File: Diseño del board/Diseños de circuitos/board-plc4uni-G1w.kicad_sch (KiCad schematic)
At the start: 0 parts

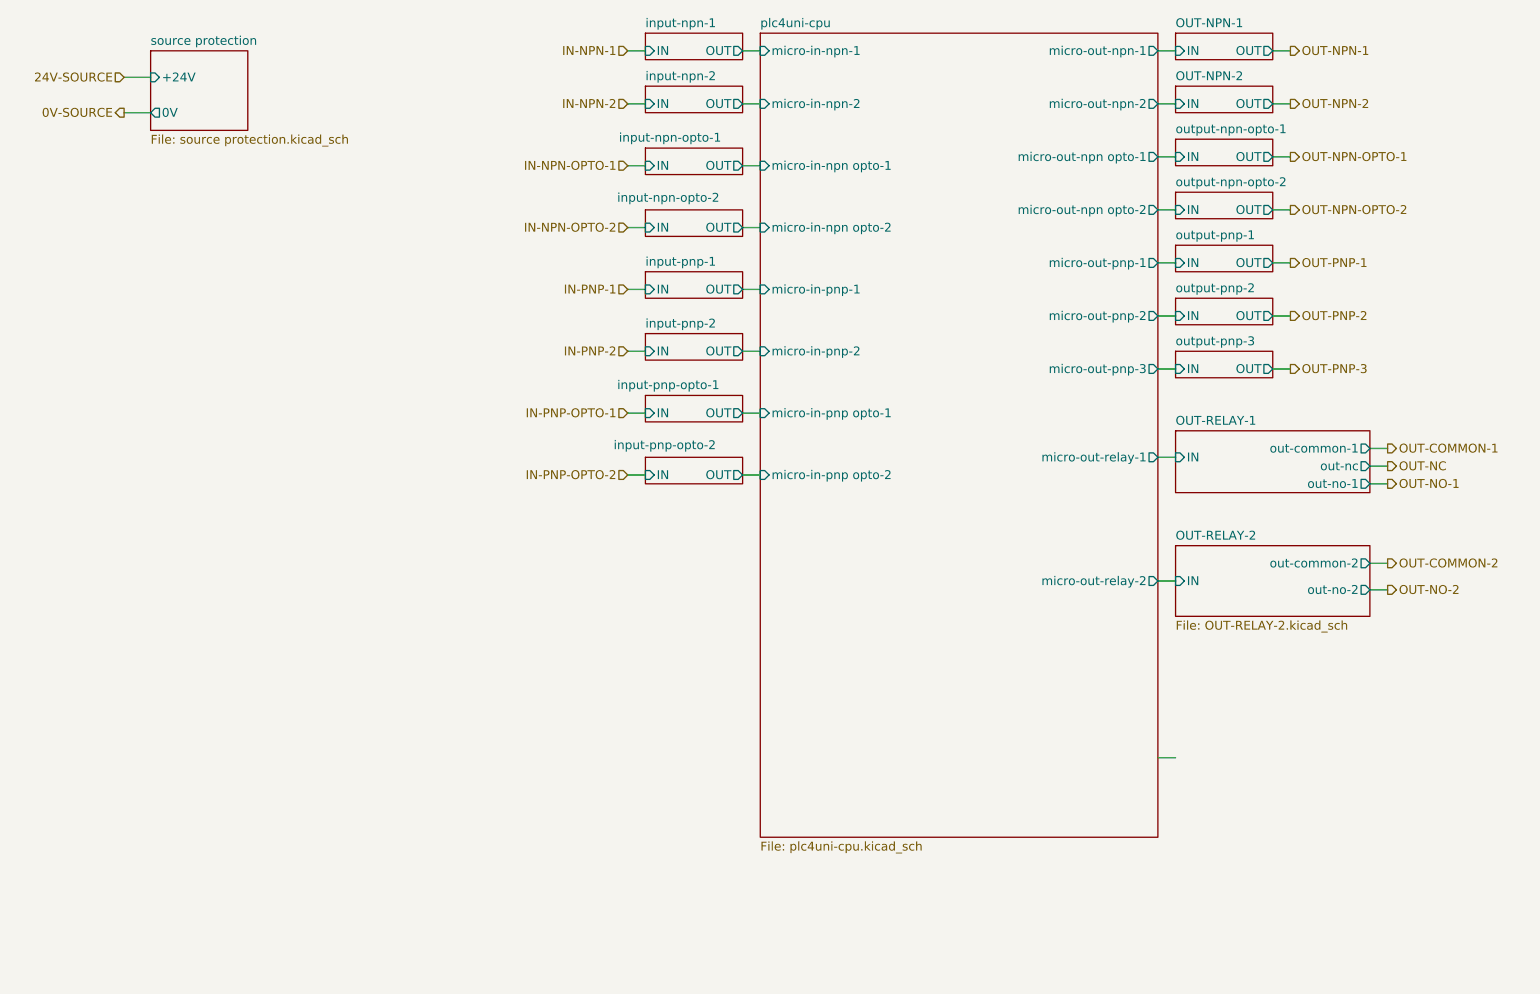
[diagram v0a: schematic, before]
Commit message: se agrego entrada y salida 0-10V
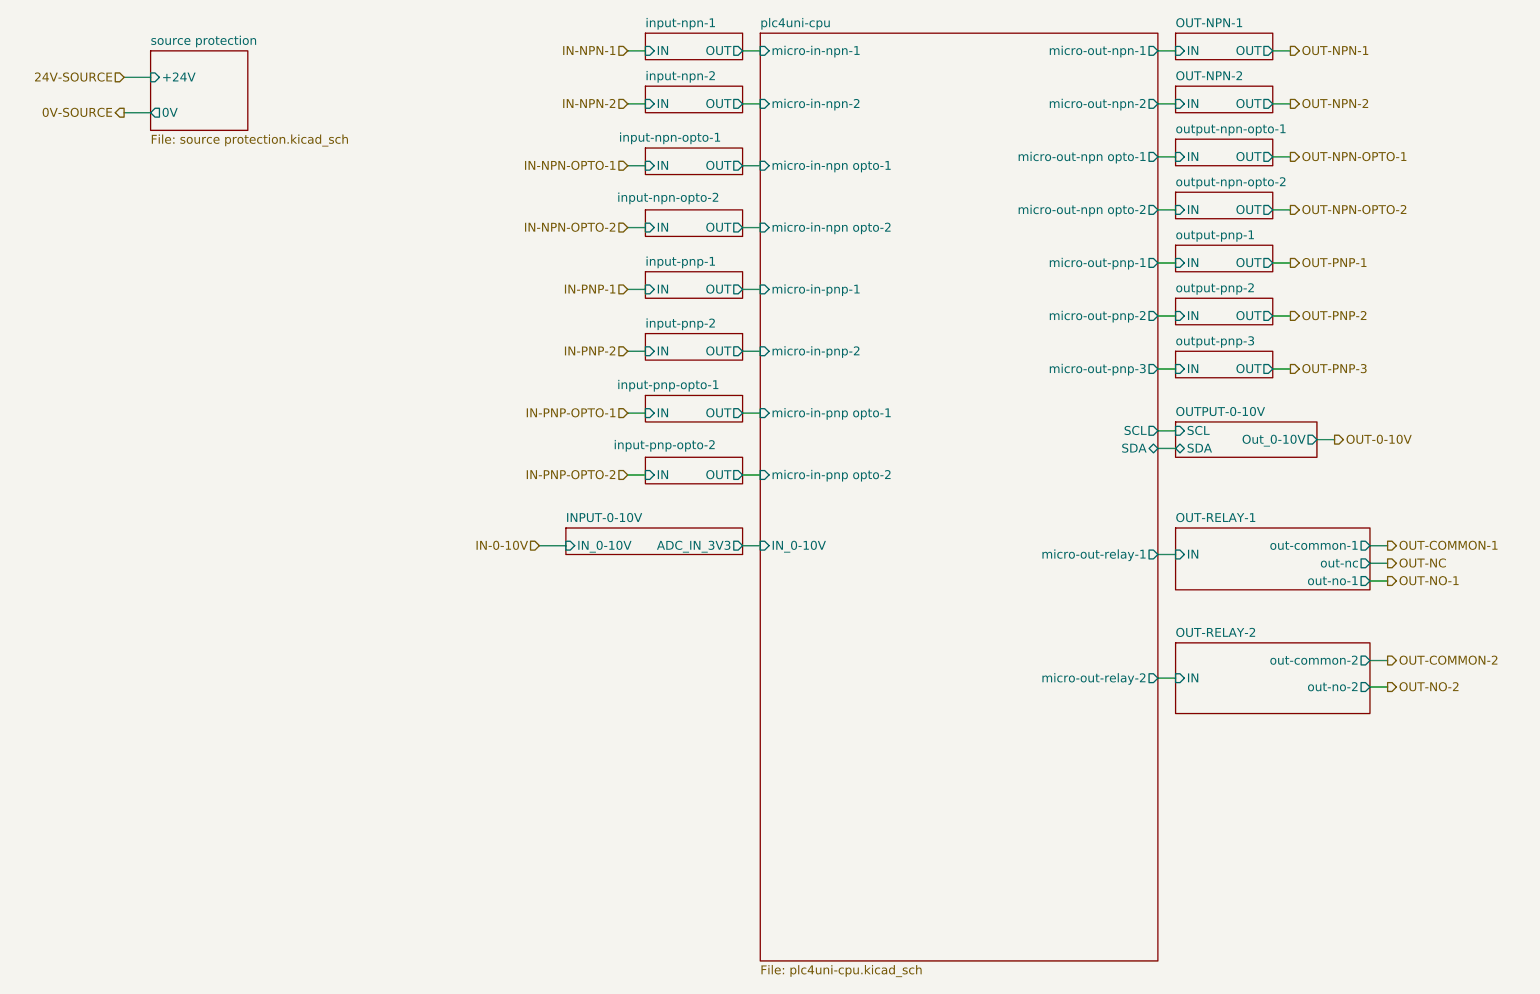
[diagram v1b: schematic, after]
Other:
- added sheet INPUT-0-10V (INPUT-0-10V.kicad_sch)
- added sheet OUTPUT-0-10V (OUTPUT-0-10V.kicad_sch)
- sheet plc4uni-cpu ports: added IN_0-10V, SCL, SDA; removed none
